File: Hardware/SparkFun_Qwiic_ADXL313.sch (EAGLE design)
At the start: 31 parts, among them J2 QWIIC_RA, J4 QWIIC_RA, U1 ADXL313

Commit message: pullup on CS for default I2C mode (aka mode jumper)
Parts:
- removed JP7: JUMPER-SMT_3_2-NC_PASTE_SILK, SparkFun-Jumpers:JUMPER-SMT_3_2-NC_PASTE_SILK
- added I2C: JUMPER-SMT_3_2-NC_TRACE_SILK, SparkFun-Jumpers:JUMPER-SMT_3_2-NC_TRACE_SILK
- added MODE: JUMPER-SMT_2_NC_TRACE_SILK, SparkFun-Jumpers:JUMPER-SMT_2_NC_TRACE_SILK
- added R1: 10k, SparkFun-Resistors:10KOHM-0603-1/10W-1%
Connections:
- new net N$3: MODE.2, R1.1
- net !CS: now also MODE.1
- net 3.3V: now also I2C.2, R1.2; no longer JP7.2
- net N$1: now also I2C.1; no longer JP7.1
- net N$2: now also I2C.3; no longer JP7.3
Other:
- note added: "Mode jumper Closed: I2C (default) Open: SPI"
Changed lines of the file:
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@@
 <part name="R4" library="SparkFun-Resistors" deviceset="4.7KOHM" device="-0603-1/10W-1%" value="4.7k"/>
 <part name="R5" library="SparkFun-Resistors" deviceset="4.7KOHM" device="-0603-1/10W-1%" value="4.7k"/>
-<part name="JP7" library="SparkFun-Jumpers" deviceset="JUMPER-SMT_3_2-NC_PASTE" device="_SILK" package3d_urn="urn:adsk.eagle:package:39294/1" value=""/>
+<part name="I2C" library="SparkFun-Jumpers" deviceset="JUMPER-SMT_3_2-NC_TRACE" device="_SILK" package3d_urn="urn:adsk.eagle:package:39289/1" value=""/>
 <part name="SUPPLY1" library="SparkFun-PowerSymbols" deviceset="3.3V" device=""/>
 <part name="SUPPLY2" library="SparkFun-PowerSymbols" deviceset="3.3V" device=""/>
@@
 <part name="C1" library="SparkFun-Capacitors" deviceset="0.1UF" device="-0603-25V-(+80/-20%)" value="0.1uF"/>
 <part name="LOGO3" library="SparkFun-Aesthetics" deviceset="SFE_LOGO_FLAME" device=".1_INCH"/>
+<part name="SUPPLY11" library="SparkFun-PowerSymbols" deviceset="3.3V" device=""/>
+<part name="R1" library="SparkFun-Resistors" deviceset="10KOHM" device="-0603-1/10W-1%" value="10k"/>
+<part name="MODE" library="SparkFun-Jumpers" deviceset="JUMPER-SMT_2_NC_TRACE" device="_SILK" package3d_urn="urn:adsk.eagle:package:39281/1" value=""/>
 </parts>
 <sheets>
@@
 <wire x1="81.28" y1="0" x2="81.28" y2="99.06" width="0.1524" layer="97" style="longdash"/>
 <wire x1="134.62" y1="0" x2="134.62" y2="99.06" width="0.1524" layer="97" style="longdash"/>
+<text x="40.64" y="162.56" size="1.778" layer="97" font="vector">Mode jumper
+Closed: I2C (default)
+Open: SPI</text>
+<wire x1="86.36" y1="152.4" x2="57.404" y2="162.814" width="0.1524" layer="97" style="shortdash"/>
 </plain>
 <instances>
@@
 <attribute name="VALUE" x="123.444" y="144.78" size="1.778" layer="96" font="vector" rot="R90" align="top-center"/>
 </instance>
-<instance part="JP7" gate="G$1" x="114.3" y="152.4" smashed="yes" rot="R270">
+<instance part="I2C" gate="G$1" x="114.3" y="152.4" smashed="yes" rot="R270">
 <attribute name="NAME" x="111.76" y="148.082" size="1.778" layer="95" font="vector"/>
 <attribute name="VALUE" x="113.919" y="149.86" size="1.778" layer="96" font="vector" rot="R270" align="top-left"/>
@@
 </instance>
 <instance part="LOGO3" gate="G$1" x="162.56" y="53.34" smashed="yes"/>
+<instance part="SUPPLY11" gate="G$1" x="93.98" y="170.18" smashed="yes">
+<attribute name="VALUE" x="93.98" y="172.974" size="1.778" layer="96" font="vector" align="bottom-center"/>
+</instance>
+<instance part="R1" gate="G$1" x="93.98" y="162.56" smashed="yes" rot="R90">
+<attribute name="NAME" x="92.456" y="162.56" size="1.778" layer="95" font="vector" rot="R90" align="bottom-center"/>
+<attribute name="VALUE" x="95.504" y="162.56" size="1.778" layer="96" font="vector" rot="R90" align="top-center"/>
+</instance>
+<instance part="MODE" gate="G$1" x="93.98" y="149.86" smashed="yes" rot="R90">
+<attribute name="NAME" x="91.44" y="147.32" size="1.778" layer="95" font="vector" rot="R90"/>
+<attribute name="VALUE" x="96.52" y="147.32" size="1.778" layer="96" font="vector" rot="R90" align="top-left"/>
+</instance>
 </instances>
 <busses>
@@
 </segment>
 <segment>
-<pinref part="JP7" gate="G$1" pin="2"/>
+<pinref part="I2C" gate="G$1" pin="2"/>
 <wire x1="114.3" y1="160.02" x2="114.3" y2="157.48" width="0.1524" layer="91"/>
 <pinref part="SUPPLY1" gate="G$1" pin="3.3V"/>
@@
 <pinref part="C1" gate="G$1" pin="1"/>
 </segment>
+<segment>
+<wire x1="93.98" y1="170.18" x2="93.98" y2="167.64" width="0.1524" layer="91"/>
+<pinref part="SUPPLY11" gate="G$1" pin="3.3V"/>
+<pinref part="R1" gate="G$1" pin="2"/>
+</segment>
 </net>
 <net name="GND" class="0">
@@
 <pinref part="R5" gate="G$1" pin="2"/>
 <wire x1="121.92" y1="149.86" x2="121.92" y2="152.4" width="0.1524" layer="91"/>
-<pinref part="JP7" gate="G$1" pin="1"/>
+<pinref part="I2C" gate="G$1" pin="1"/>
 <wire x1="121.92" y1="152.4" x2="119.38" y2="152.4" width="0.1524" layer="91"/>
 </segment>
@@
 <pinref part="R4" gate="G$1" pin="2"/>
 <wire x1="106.68" y1="149.86" x2="106.68" y2="152.4" width="0.1524" layer="91"/>
-<pinref part="JP7" gate="G$1" pin="3"/>
+<pinref part="I2C" gate="G$1" pin="3"/>
 <wire x1="106.68" y1="152.4" x2="109.22" y2="152.4" width="0.1524" layer="91"/>
 </segment>
@@
 <segment>
 <wire x1="91.44" y1="142.24" x2="93.98" y2="142.24" width="0.1524" layer="91"/>
-<label x="93.98" y="142.24" size="1.27" layer="95" font="vector" xref="yes"/>
+<label x="96.52" y="142.24" size="1.27" layer="95" font="vector" xref="yes"/>
 <pinref part="U1" gate="G$1" pin="!CS"/>
+<pinref part="MODE" gate="G$1" pin="1"/>
+<wire x1="93.98" y1="142.24" x2="96.52" y2="142.24" width="0.1524" layer="91"/>
+<wire x1="93.98" y1="142.24" x2="93.98" y2="144.78" width="0.1524" layer="91"/>
+<junction x="93.98" y="142.24"/>
 </segment>
 </net>
@@
 </segment>
 </net>
+<net name="N$3" class="0">
+<segment>
+<pinref part="MODE" gate="G$1" pin="2"/>
+<pinref part="R1" gate="G$1" pin="1"/>
+<wire x1="93.98" y1="154.94" x2="93.98" y2="157.48" width="0.1524" layer="91"/>
+</segment>
+</net>

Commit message: routing done
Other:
- note added: "v10"
- note removed: "v01"
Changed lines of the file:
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@@
 <text x="193.04" y="132.08" size="1.778" layer="97" font="vector">Open (default) = 0x1D</text>
 <text x="170.434" y="11.43" size="2.54" layer="94" font="vector">Pete Lewis</text>
-<text x="237.744" y="7.366" size="2.54" layer="94" font="vector">v01</text>
+<text x="237.744" y="7.366" size="2.54" layer="94" font="vector">v10</text>
 <wire x1="0" y1="99.06" x2="81.28" y2="99.06" width="0.1524" layer="97" style="longdash"/>
 <text x="7.62" y="177.8" size="2.54" layer="94" font="vector">ADXL313 Accelerometer</text>

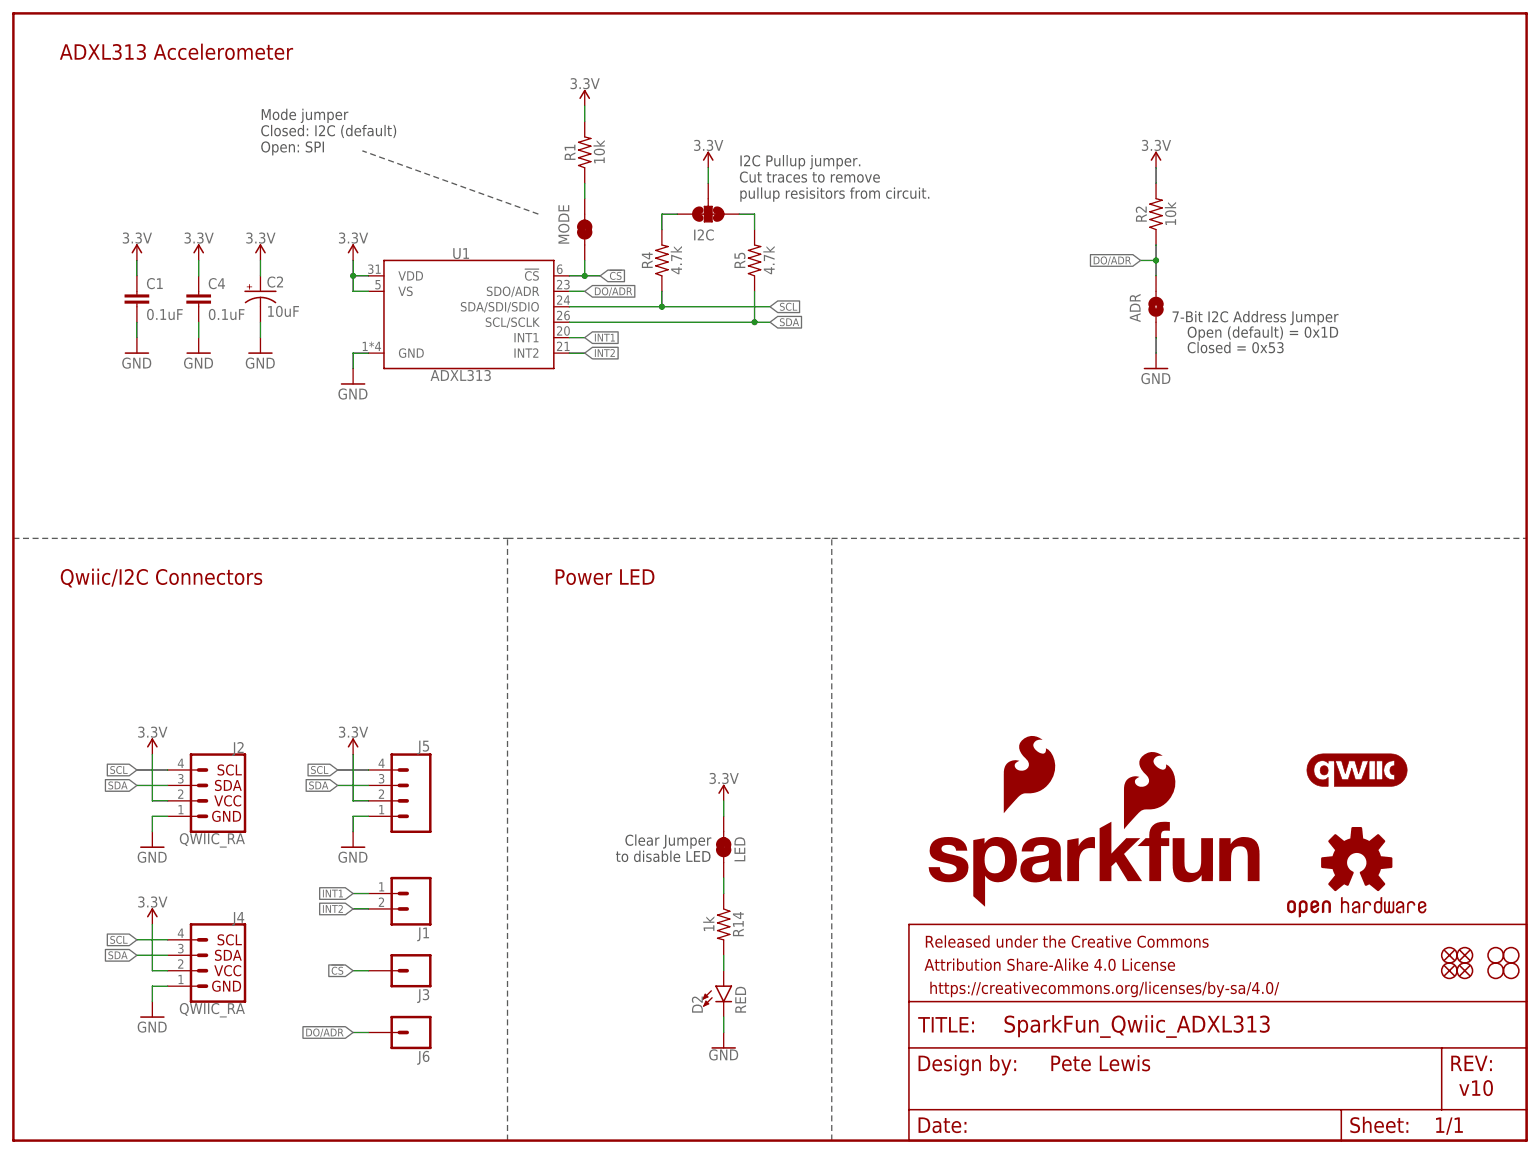
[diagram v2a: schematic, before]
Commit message: ENG checklist run changes - pre-group review
-sch cleanup
-PROD_ID for IC
-GND stiching vias and re-routed 3.3V near IC for better GND return path from filter caps
-approve DRC errors (jumper overlaps and some stubs)
-more measures
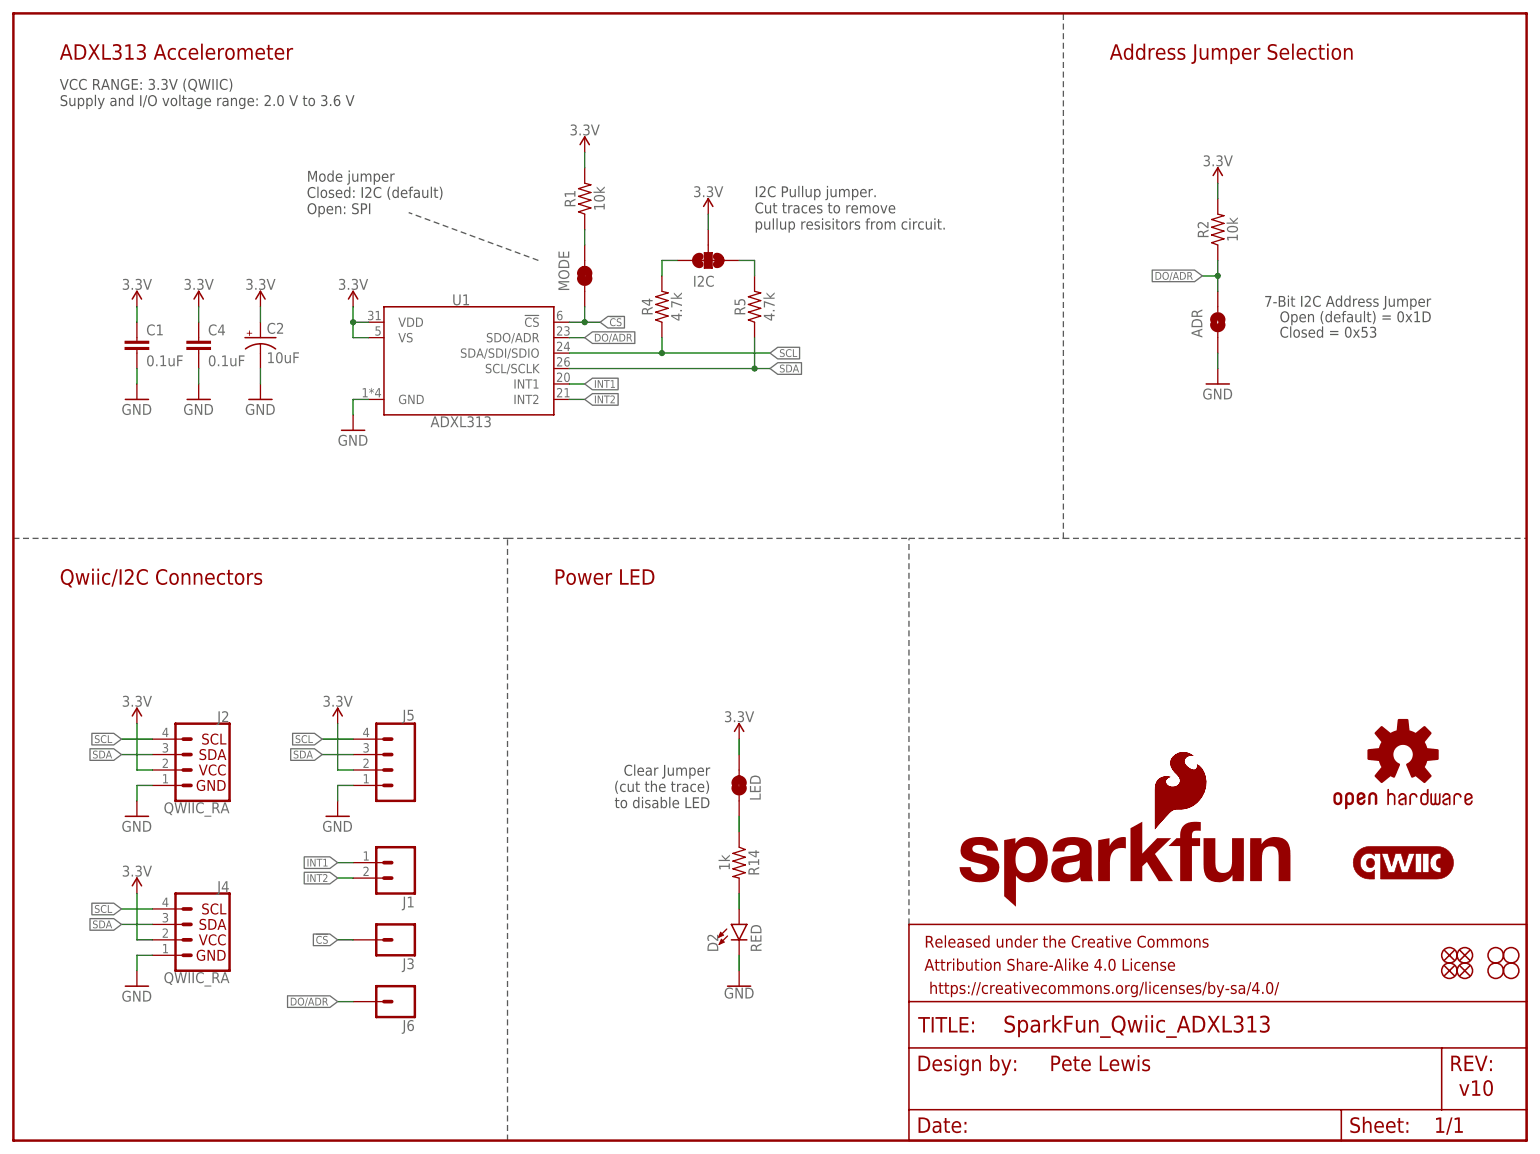
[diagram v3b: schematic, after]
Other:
- note added: "Address Jumper Selection"
- note added: "Clear Jumper (cut the trace) to disable LED"
- note added: "VCC RANGE: 3.3V (QWIIC) Supply and I/O voltage range: 2.0 V to 3.6 V"
- note removed: "Clear Jumper to disable LED"
- moved on the sheet: ADR, C1, C2, C4, D2, I2C, J1, J2, J3, J4, J5, J6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

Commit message: Group Review changes
-Removed MODE Jumper, CS should always be tied high.
-Added optional Resistor on power input to IC, for potential RC filter.
-SDA/SCL corrected
- corrected pin location in device footprint. (they were mirrored)
- 3 vias under IC are now actually named GND
- CS and SDO were swapped with INTs so all data lines are on the same row of headers
- End caps on buzzards corrected.
- Moved to all I2C labels on top and SPI labels on bottom.
- added tRestrict near pads on IC to stop gdn flow on top corner and natural jumper of two inner GND pads.
- Symbol now has NC pin and Reserved pin
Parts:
- removed C1: 0.1uF, SparkFun-Capacitors:0.1UF-0603-25V-(+80/-20%)
- removed J3, J6: (no value), SparkFun-Connectors:CONN_01PTH_NO_SILK_YES_STOP
- removed MODE: JUMPER-SMT_2_NC_TRACE_SILK, SparkFun-Jumpers:JUMPER-SMT_2_NC_TRACE_SILK
- removed R14: 1k, SparkFun-Resistors:1KOHM-0603-1/10W-1%
- added J7: (no value), SparkFun-Connectors:CONN_021X02_NO_SILK
- added R3: 4.7k, SparkFun-Resistors:4.7KOHM-0603-1/10W-1%
- added R6: 0, SparkFun-Resistors:0OHM-0603-1/10W
- R5: value 4.7k -> 1k; device SparkFun-Resistors:4.7KOHM-0603-1/10W-1% -> SparkFun-Resistors:1KOHM-0603-1/10W-1%
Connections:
- removed net DO/ADR: ADR.2, J6.1, R2.1, U1.SDO/ADR
- new net SDO/ADR: ADR.2, J7.2, R2.1, U1.SDO/ADR
- net !CS: now also J7.1, R1.1; no longer J3.1, MODE.1
- net 3.3V: now also R6.1; no longer C1.1, C2.+, C4.1, U1.VDD, U1.VS
- net GND: no longer C1.2
- net N$1: now also R3.2; no longer R5.2
- net N$3: now also C2.+, C4.1, R6.2, U1.VDD, U1.VS; no longer MODE.2, R1.1
- net N$6: now also R5.2; no longer R14.2
- net N$8: now also R5.1; no longer R14.1
- net SCL: now also U1.SCL/SCLK; no longer U1.SDA/SDI/SDIO
- net SDA: now also R3.1, U1.SDA/SDI/SDIO; no longer R5.1, U1.SCL/SCLK
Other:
- note removed: "Mode jumper Closed: I2C (default) Open: SPI"
- moved on the sheet: C2, C4, R1, R5

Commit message: replaced ADXL313 with device in main eagle Sensor library
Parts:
- U1: device adxl313:ADXL313 -> SparkFun-Sensors:ADXL313
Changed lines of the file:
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@@
 <setting verticaltext="up"/>
 </settings>
-<grid distance="0.1" unitdist="inch" unit="inch" style="lines" multiple="1" display="no" altdistance="0.001" altunitdist="inch" altunit="inch"/>
+<grid distance="0.1" unitdist="inch" unit="inch" style="lines" multiple="1" display="no" altdistance="0.01" altunitdist="inch" altunit="inch"/>
 <layers>
 <layer number="1" name="Top" color="4" fill="1" visible="no" active="no"/>
@@
 <layer number="128" name="_bValues" color="7" fill="1" visible="yes" active="yes"/>
 <layer number="129" name="Mask" color="7" fill="1" visible="yes" active="yes"/>
+<layer number="130" name="SMDSTROOK" color="7" fill="1" visible="no" active="no"/>
 <layer number="131" name="tAdjust" color="7" fill="1" visible="yes" active="yes"/>
 <layer number="132" name="bAdjust" color="7" fill="1" visible="yes" active="yes"/>
+<layer number="133" name="bottom_silk" color="7" fill="1" visible="no" active="no"/>
+<layer number="134" name="silk_top" color="7" fill="1" visible="no" active="no"/>
+<layer number="135" name="silk_bottom" color="7" fill="1" visible="no" active="no"/>
+<layer number="136" name="silktop" color="7" fill="1" visible="no" active="no"/>
+<layer number="137" name="silkbottom" color="7" fill="1" visible="no" active="no"/>
+<layer number="138" name="EEE" color="7" fill="1" visible="no" active="no"/>
+<layer number="139" name="_tKeepout" color="7" fill="1" visible="no" active="no"/>
+<layer number="140" name="mbKeepout" color="7" fill="1" visible="no" active="no"/>
+<layer number="141" name="ASSEMBLY_TOP" color="7" fill="1" visible="no" active="no"/>
+<layer number="142" name="mbRestrict" color="7" fill="1" visible="no" active="no"/>
+<layer number="143" name="PLACE_BOUND_TOP" color="7" fill="1" visible="no" active="no"/>
 <layer number="144" name="Drill_legend" color="7" fill="1" visible="yes" active="yes"/>
+<layer number="145" name="DrillLegend_01-16" color="7" fill="1" visible="no" active="no"/>
+<layer number="146" name="DrillLegend_01-20" color="7" fill="1" visible="no" active="no"/>
+<layer number="147" name="PIN_NUMBER" color="7" fill="1" visible="no" active="no"/>
+<layer number="149" name="DrillLegend_02-15" color="7" fill="1" visible="no" active="no"/>
 <layer number="150" name="Notes" color="7" fill="1" visible="yes" active="yes"/>
 <layer number="151" name="HeatSink" color="7" fill="1" visible="yes" active="yes"/>
@@
 <layer number="154" name="FabDoc2" color="7" fill="1" visible="yes" active="yes"/>
 <layer number="155" name="FabDoc3" color="7" fill="1" visible="yes" active="yes"/>
+<layer number="166" name="AntennaArea" color="7" fill="1" visible="no" active="no"/>
+<layer number="168" name="4mmHeightArea" color="7" fill="1" visible="no" active="no"/>
+<layer number="191" name="mNets" color="7" fill="1" visible="no" active="no"/>
+<layer number="192" name="mBusses" color="7" fill="1" visible="no" active="no"/>
+<layer number="193" name="mPins" color="7" fill="1" visible="no" active="no"/>
+<layer number="194" name="mSymbols" color="7" fill="1" visible="no" active="no"/>
+<layer number="195" name="mNames" color="7" fill="1" visible="no" active="no"/>
+<layer number="196" name="mValues" color="7" fill="1" visible="no" active="no"/>
 <layer number="199" name="Contour" color="7" fill="1" visible="yes" active="yes"/>
 <layer number="200" name="200bmp" color="1" fill="10" visible="yes" active="yes"/>
@@
 <part name="C2" library="SparkFun-Retired" deviceset="10UF-TANT" device="" value="10uF"/>
 <part name="ADR" library="SparkFun-Jumpers" deviceset="JUMPER-SMT_2_NO" device="_SILK" package3d_urn="urn:adsk.eagle:package:39279/1" value=""/>
-<part name="U1" library="adxl313" deviceset="ADXL313" device=""/>
+<part name="U1" library="SparkFun-Sensors" deviceset="ADXL313" device=""/>
 <part name="D2" library="SparkFun-LED" deviceset="LED-RED" device="0603" value="RED"/>
 <part name="R5" library="SparkFun-Resistors" deviceset="1KOHM" device="-0603-1/10W-1%" value="1k"/>
